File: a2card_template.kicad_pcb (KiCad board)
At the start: 2 copper layers, 158.8 x 76.4 mm, 1 part

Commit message: Synchronized edge with schematic
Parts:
- BUS1: value Apple -> Connector_Apple-Apple_ii_68008-cache
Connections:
- net +5V renamed Net-(BUS1-Pad25)
- net /7MHz renamed Net-(BUS1-Pad36)
- net /A0_SLOT renamed Net-(BUS1-Pad2)
- net /A10_SLOT renamed Net-(BUS1-Pad12)
- net /A11_SLOT renamed Net-(BUS1-Pad13)
- net /A12_SLOT renamed Net-(BUS1-Pad14)
- net /A13_SLOT renamed Net-(BUS1-Pad15)
- net /A14_SLOT renamed Net-(BUS1-Pad16)
- net /A15_SLOT renamed Net-(BUS1-Pad17)
- net /A1_SLOT renamed Net-(BUS1-Pad3)
- net /A2_SLOT renamed Net-(BUS1-Pad4)
- net /A3_SLOT renamed Net-(BUS1-Pad5)
- net /A4_SLOT renamed Net-(BUS1-Pad6)
- net /A5_SLOT renamed Net-(BUS1-Pad7)
- net /A6_SLOT renamed Net-(BUS1-Pad8)
- net /A7_SLOT renamed Net-(BUS1-Pad9)
- net /A8_SLOT renamed Net-(BUS1-Pad10)
- net /A9_SLOT renamed Net-(BUS1-Pad11)
- net /D0_SLOT renamed Net-(BUS1-Pad49)
- net /D1_SLOT renamed Net-(BUS1-Pad48)
- net /D2_SLOT renamed Net-(BUS1-Pad47)
- net /D3_SLOT renamed Net-(BUS1-Pad46)
- net /D4_SLOT renamed Net-(BUS1-Pad45)
- net /D5_SLOT renamed Net-(BUS1-Pad44)
- net /D6_SLOT renamed Net-(BUS1-Pad43)
- net /D7_SLOT renamed Net-(BUS1-Pad42)
- net /DMA# renamed Net-(BUS1-Pad22)
- net /IOSEL# renamed Net-(BUS1-Pad1)
- net /PHI_0 renamed Net-(BUS1-Pad40)
- net /PHI_1 renamed Net-(BUS1-Pad38)
- net /Q3 renamed Net-(BUS1-Pad37)
- net /RESET# renamed Net-(BUS1-Pad31)
- net /RW# renamed Net-(BUS1-Pad18)
- net GND renamed Net-(BUS1-Pad26)
- BUS1 pad 21: /DMA_OUT -> Net-(BUS1-Pad21)
- BUS1 pad 24: /DMA_OUT -> Net-(BUS1-Pad24)
- BUS1 pad 28: Net-(BUS1-Pad23) -> Net-(BUS1-Pad28)

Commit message: Silk repair
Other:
- board text added: "2021 by leadedsolder.com"
- board text added: "Apple II Z80 SoftCard Clone v0.1"
- board text added: "special thanks to plpg"
- board text removed: "0"
- board text removed: "2"
- board text removed: "BERR"
- board text removed: "CPU_HALT"
- board text removed: "CPU_RESET"
- board text removed: "CoPro-8MC"
- board text removed: "FUNCTION CODE"
- board text removed: "VPA"
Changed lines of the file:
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@@
   (general
     (thickness 1.6)
-    (drawings 27)
+    (drawings 20)
     (tracks 0)
     (zones 0)
@@
     (0 F.Cu signal)
     (31 B.Cu signal)
-    (32 B.Adhes user hide)
-    (33 F.Adhes user hide)
-    (34 B.Paste user hide)
-    (35 F.Paste user hide)
-    (36 B.SilkS user hide)
-    (37 F.SilkS user hide)
-    (38 B.Mask user hide)
-    (39 F.Mask user hide)
-    (40 Dwgs.User user hide)
+    (32 B.Adhes user)
+    (33 F.Adhes user)
+    (34 B.Paste user)
+    (35 F.Paste user)
+    (36 B.SilkS user)
+    (37 F.SilkS user)
+    (38 B.Mask user)
+    (39 F.Mask user)
+    (40 Dwgs.User user)
     (41 Cmts.User user)
-    (42 Eco1.User user hide)
-    (43 Eco2.User user hide)
+    (42 Eco1.User user)
+    (43 Eco2.User user)
     (44 Edge.Cuts user)
-    (45 Margin user hide)
-    (46 B.CrtYd user hide)
-    (47 F.CrtYd user hide)
-    (48 B.Fab user hide)
-    (49 F.Fab user hide)
+    (45 Margin user)
+    (46 B.CrtYd user)
+    (47 F.CrtYd user)
+    (48 B.Fab user)
+    (49 F.Fab user)
   )
   (setup
@@
   (module Apple_ii_card:AppleII_card_edge (layer F.Cu)
     (at 185.74 125.39)
-    (fp_text reference BUS1 (at -30.48 -1.27) (layer F.SilkS)
+    (fp_text reference BUS1 (at -30.48 -1.27) (layer F.SilkS) hide
       (effects (font (size 1 1) (thickness 0.15)))
     )
@@
       (effects (font (size 1 1) (thickness 0.15)))
     )
+    (fp_line (start -33.02 7.62) (end -33.02 0) (layer F.Fab) (width 0.15))
+    (fp_line (start 33.02 7.62) (end -33.02 7.62) (layer F.Fab) (width 0.15))
     (fp_line (start 33.02 0) (end 33.02 7.62) (layer F.Fab) (width 0.15))
-    (fp_line (start 33.02 7.62) (end -33.02 7.62) (layer F.Fab) (width 0.15))
-    (fp_line (start -33.02 7.62) (end -33.02 0) (layer F.Fab) (width 0.15))
     (pad 50 smd rect (at -30.48 3.81) (size 1.27 7.62) (layers F.Cu F.Paste F.Mask)
       (net 13 "Net-(BUS1-Pad50)"))
@@
       (net 50 "Net-(BUS1-Pad1)"))
   )
+  (gr_text "special thanks to plpg" (at 226.6696 59.1058) (layer F.SilkS)
+    (effects (font (size 2 2) (thickness 0.15)) (justify right))
+  )
+  (gr_text "2021 by leadedsolder.com" (at 111.6838 62.0268) (layer F.SilkS)
+    (effects (font (size 1 1) (thickness 0.15)))
+  )
+  (gr_text "Apple II Z80 SoftCard Clone v0.1" (at 96.4692 59.8678) (layer F.SilkS)
+    (effects (font (size 2 2) (thickness 0.15)))
+  )
   (dimension 9.6 (width 0.15) (layer Cmts.User)
     (gr_text "9,600 mm" (at 223.5 147.858) (layer Cmts.User)
@@
     (effects (font (size 1.5 1.5) (thickness 0.3) italic))
   )
-  (gr_text "FUNCTION CODE" (at 151.892 62.992) (layer F.SilkS)
-    (effects (font (size 1.2 1.2) (thickness 0.3)))
-  )
-  (gr_text CoPro-8MC (at 98.552 62.484) (layer F.SilkS)
-    (effects (font (size 3 3) (thickness 0.75)))
-  )
-  (gr_line (start 132.08 61.468) (end 132.08 70.612) (layer F.SilkS) (width 0.3))
-  (gr_line (start 126.492 61.468) (end 126.492 71.628) (layer F.SilkS) (width 0.3))
-  (gr_text VPA (at 135.636 63.246 -90) (layer F.SilkS)
-    (effects (font (size 1.2 1.2) (thickness 0.3)))
-  )
-  (gr_text CPU_HALT (at 130.556 66.04 -90) (layer F.SilkS)
-    (effects (font (size 1.2 1.2) (thickness 0.3)))
-  )
-  (gr_text CPU_RESET (at 124.968 66.548 -90) (layer F.SilkS)
-    (effects (font (size 1.2 1.2) (thickness 0.3)))
-  )
-  (gr_text BERR (at 119.888 64.516 270) (layer F.SilkS)
-    (effects (font (size 1.5 1.5) (thickness 0.3125)))
-  )
-  (gr_text 2 (at 160.02 59.436) (layer F.SilkS)
-    (effects (font (size 1 1) (thickness 0.25)))
-  )
-  (gr_text 0 (at 143.764 59.436) (layer F.SilkS)
-    (effects (font (size 1 1) (thickness 0.25)))
-  )
   (gr_text "--> via 0.8mm/0.4mm" (at 72.04 26.848) (layer Cmts.User)

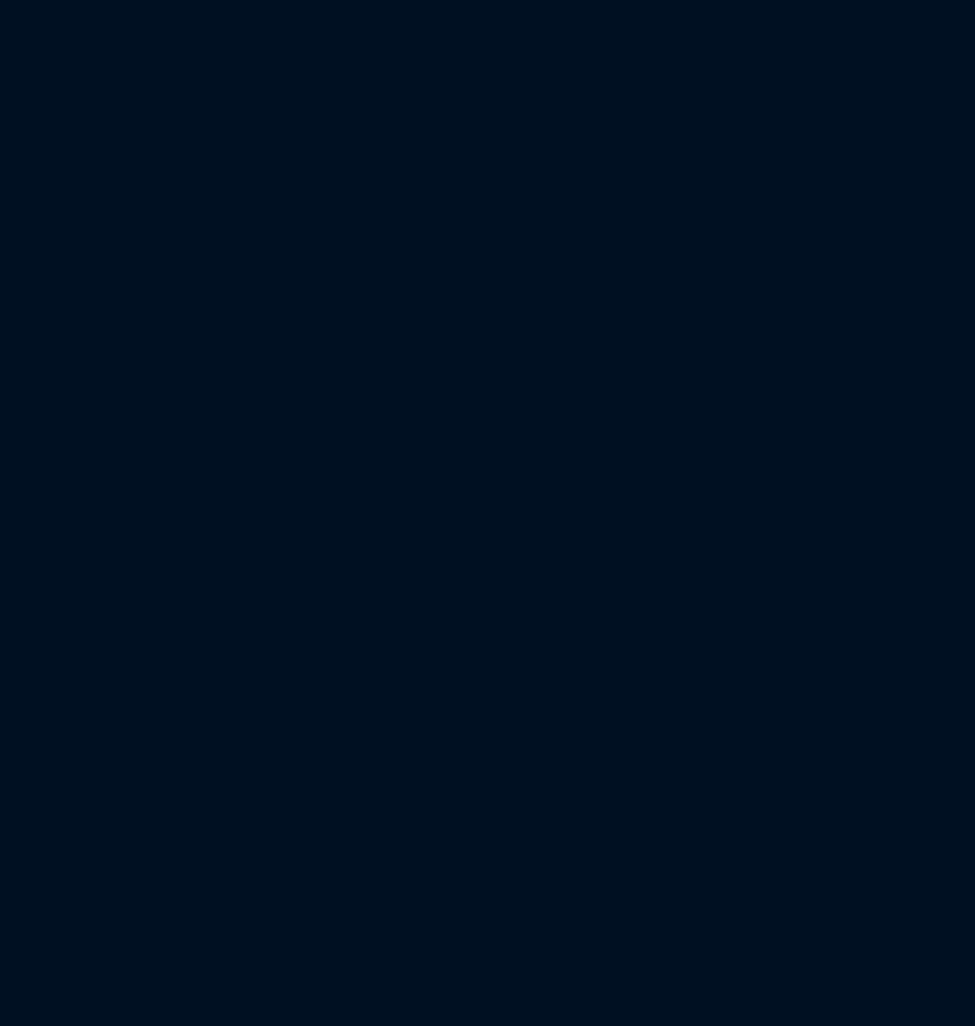
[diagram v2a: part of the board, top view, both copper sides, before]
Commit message: Landed the Leako PLCC Z80
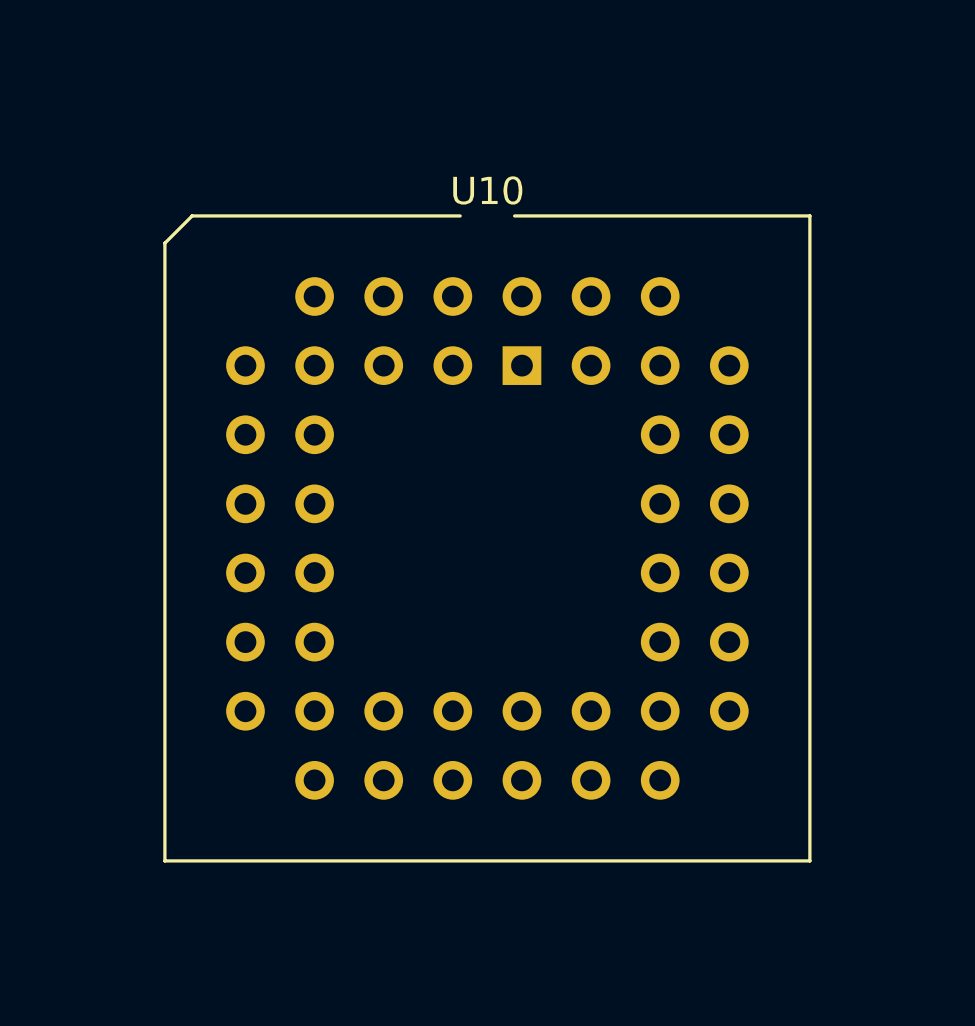
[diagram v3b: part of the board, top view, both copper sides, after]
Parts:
- added U10: PLCCZ80, Package_LCC:PLCC-44_THT-Socket, F.Cu at (148.6, 85.5)

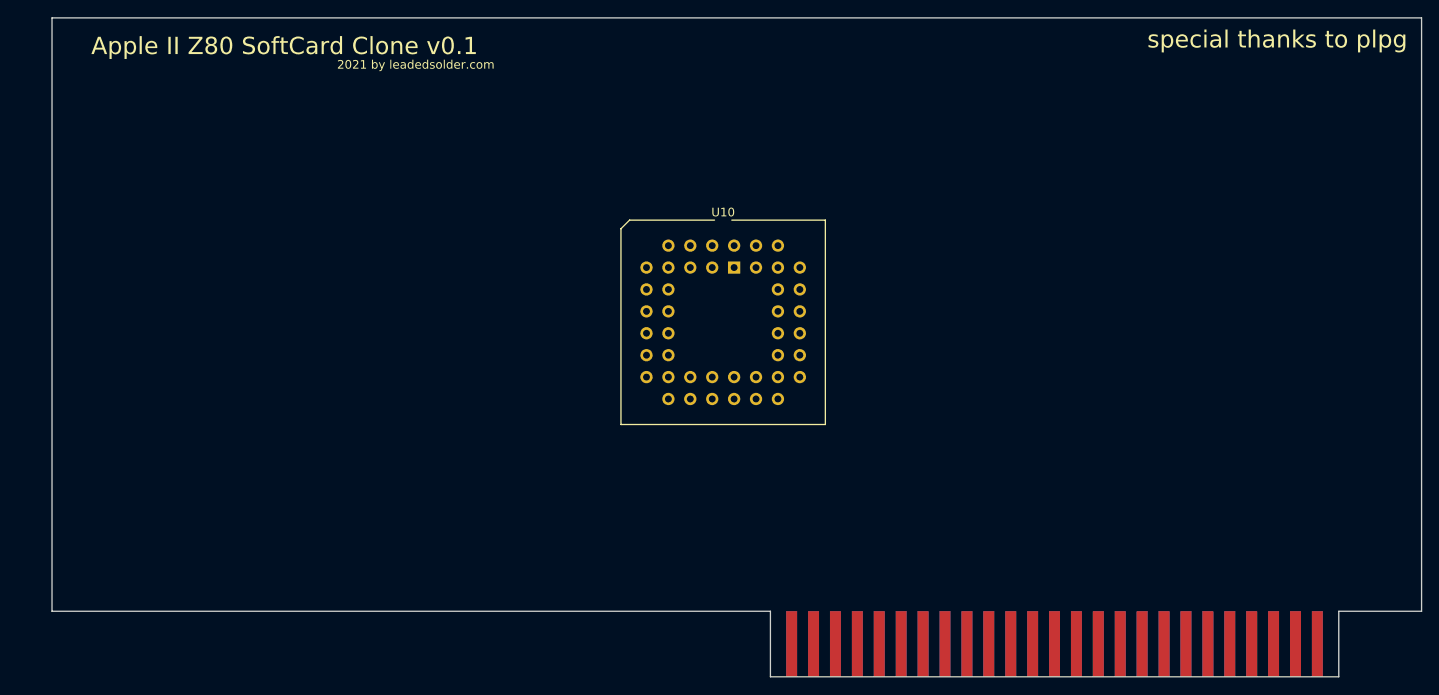
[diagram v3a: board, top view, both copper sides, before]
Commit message: Filling in the schemaitc
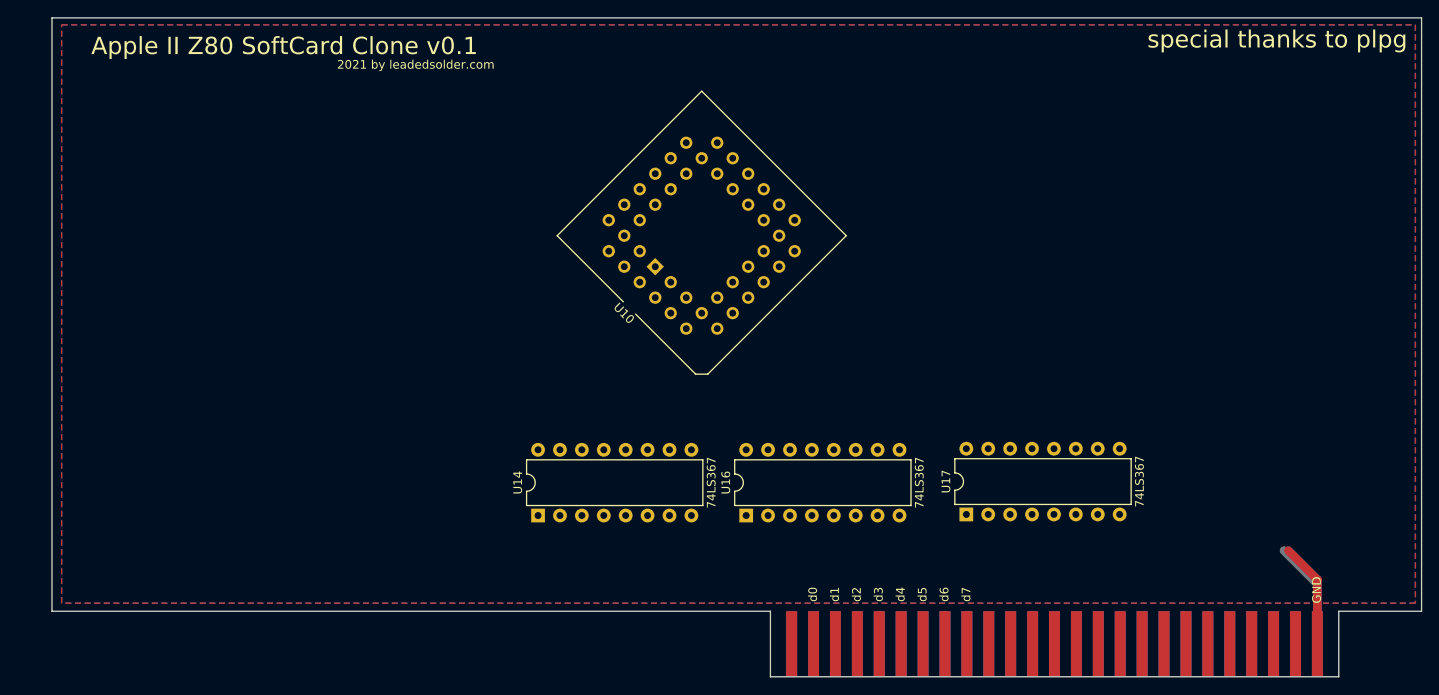
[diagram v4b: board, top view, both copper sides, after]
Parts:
- added U14: 74LS367, Package_DIP:DIP-16_W7.62mm, F.Cu at (125.9, 114.3)
- added U16: 74LS367, Package_DIP:DIP-16_W7.62mm, F.Cu at (150.0, 114.3)
- added U17: 74LS367, Package_DIP:DIP-16_W7.62mm, F.Cu at (175.5, 114.2)
- moved U10 9.14 mm to (139.4, 85.4), turned to 135 degrees
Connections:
- net Net-(BUS1-Pad42) renamed /d7
- net Net-(BUS1-Pad43) renamed /d6
- net Net-(BUS1-Pad44) renamed /d5
- net Net-(BUS1-Pad45) renamed /d4
- net Net-(BUS1-Pad46) renamed /d3
- net Net-(BUS1-Pad47) renamed /d2
- net Net-(BUS1-Pad48) renamed /d1
- net Net-(BUS1-Pad49) renamed /d0
- BUS1 pad 10: Net-(BUS1-Pad10) -> /a8
- BUS1 pad 11: Net-(BUS1-Pad11) -> /a9
- BUS1 pad 12: Net-(BUS1-Pad12) -> /a10
- BUS1 pad 13: Net-(BUS1-Pad13) -> /a11
- BUS1 pad 14: Net-(BUS1-Pad14) -> /a12
- BUS1 pad 15: Net-(BUS1-Pad15) -> /a13
- BUS1 pad 16: Net-(BUS1-Pad16) -> /a14
- BUS1 pad 17: Net-(BUS1-Pad17) -> /a15
- BUS1 pad 2: Net-(BUS1-Pad2) -> /a0
- BUS1 pad 25: Net-(BUS1-Pad25) -> +5V
- BUS1 pad 26: Net-(BUS1-Pad26) -> GND
- BUS1 pad 3: Net-(BUS1-Pad3) -> /a1
- BUS1 pad 4: Net-(BUS1-Pad4) -> /a2
- BUS1 pad 5: Net-(BUS1-Pad5) -> /a3
- BUS1 pad 6: Net-(BUS1-Pad6) -> /a4
- BUS1 pad 7: Net-(BUS1-Pad7) -> /a5
- BUS1 pad 8: Net-(BUS1-Pad8) -> /a6
- BUS1 pad 9: Net-(BUS1-Pad9) -> /a7
- U10 pad 1: Net-(U10-Pad1) -> /a11'
- U10 pad 13: Net-(U10-Pad13) -> +5V
- U10 pad 2: Net-(U10-Pad2) -> /a12'
- U10 pad 3: Net-(U10-Pad3) -> /a13'
- U10 pad 33: Net-(U10-Pad33) -> GND
- U10 pad 34: Net-(U10-Pad34) -> /a0'
- U10 pad 35: Net-(U10-Pad35) -> /a1'
- U10 pad 36: Net-(U10-Pad36) -> /a2'
- U10 pad 37: Net-(U10-Pad37) -> /a3'
- U10 pad 38: Net-(U10-Pad38) -> /a4'
- U10 pad 39: Net-(U10-Pad39) -> /a5'
- U10 pad 4: Net-(U10-Pad4) -> /a14'
- U10 pad 40: Net-(U10-Pad40) -> /a6'
- U10 pad 41: Net-(U10-Pad41) -> /a7'
- U10 pad 42: Net-(U10-Pad42) -> /a8'
- U10 pad 43: Net-(U10-Pad43) -> /a9'
- U10 pad 44: Net-(U10-Pad44) -> /a10'
- U10 pad 5: Net-(U10-Pad5) -> /a15'
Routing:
- net +5V: track 0.00 -> 12.4 mm
- net GND: track 0.00 -> 12.2 mm
- added copper zone on B.Cu, net +5V
- added copper zone on F.Cu, net GND
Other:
- board text added: "+5V"
- board text added: "GND"
- board text added: "a0"
- board text added: "a1"
- board text added: "a10"
- board text added: "a11"
- board text added: "a12"
- board text added: "a13"
- board text added: "a14"
- board text added: "a15"
- board text added: "a2"
- board text added: "a3"
- board text added: "a4"
- board text added: "a5"
- board text added: "a6"
- board text added: "a7"
- board text added: "a8"
- board text added: "a9"
- board text added: "d0"
- board text added: "d1"
- board text added: "d2"
- board text added: "d3"
- board text added: "d4"
- board text added: "d5"
- board text added: "d6"
- board text added: "d7"

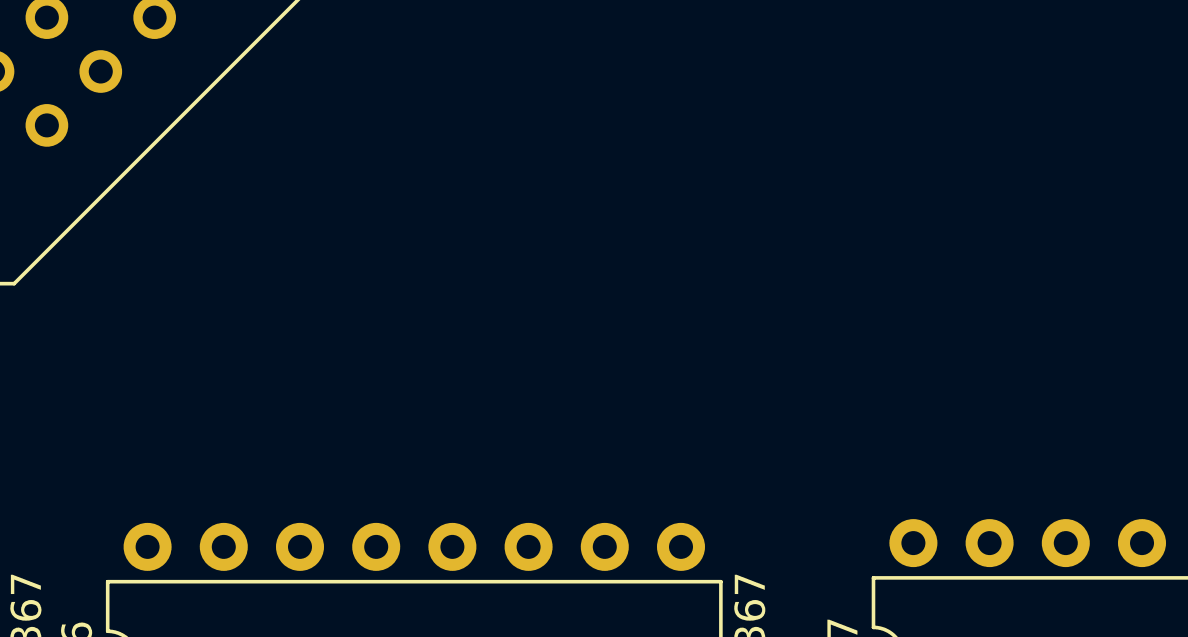
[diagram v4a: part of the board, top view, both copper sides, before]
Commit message: Add data-bus latch
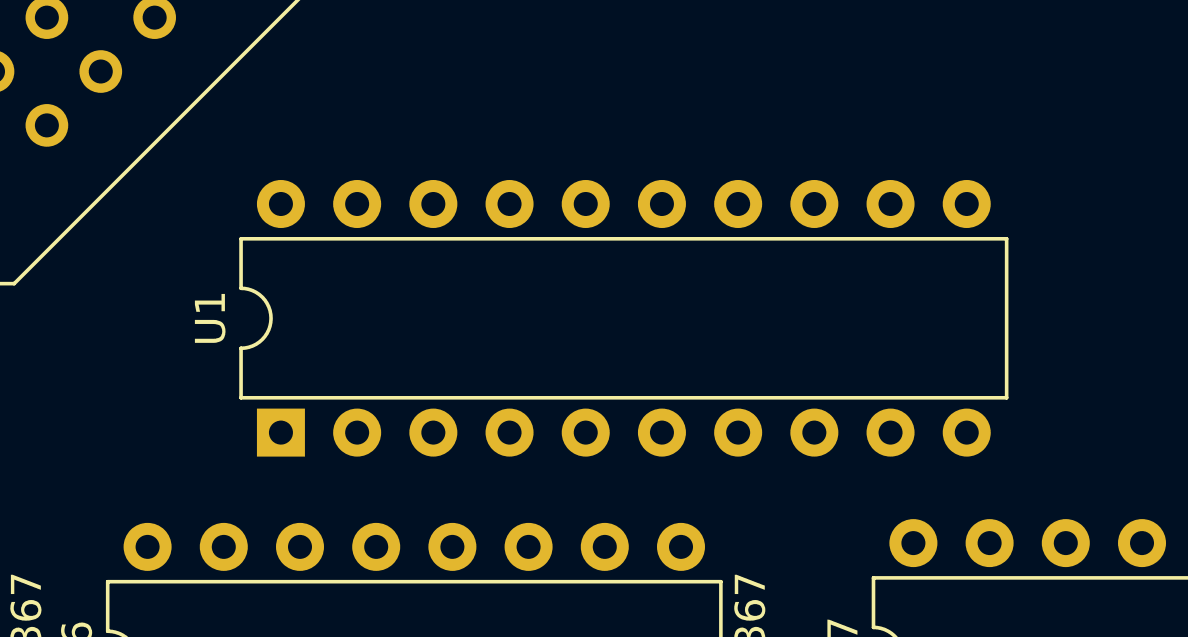
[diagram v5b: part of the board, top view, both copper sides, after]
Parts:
- added U1: 74LS373, Package_DIP:DIP-20_W7.62mm, F.Cu at (154.4, 102.9)
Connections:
- BUS1 pad 40: Net-(BUS1-Pad40) -> /ø0
- U10 pad 10: Net-(U10-Pad10) -> /d5'
- U10 pad 11: Net-(U10-Pad11) -> /d6'
- U10 pad 14: Net-(U10-Pad14) -> /d2'
- U10 pad 15: Net-(U10-Pad15) -> /d7'
- U10 pad 16: Net-(U10-Pad16) -> /d0'
- U10 pad 17: Net-(U10-Pad17) -> /d1'
- U10 pad 23: Net-(U10-Pad23) -> /~RD
- U10 pad 8: Net-(U10-Pad8) -> /d4'
- U10 pad 9: Net-(U10-Pad9) -> /d3'
